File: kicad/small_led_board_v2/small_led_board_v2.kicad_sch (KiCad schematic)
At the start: 83 parts, among them Q1 SQ2351CES, Q2 SQ2351CES, Q3 SQ2351CES, Q4 SQ2351CES, Q5 SQ2351CES, Q6 SQ2351CES, U1 TPIC6B595N, U2 74HCT595, U3 74AHCT541

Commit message: small led board v2: schematics done for now
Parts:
- C1: renamed from C4; footprint (none) -> Capacitor_THT:C_Disc_D4.7mm_W2.5mm_P5.00mm
- C2: renamed from C1; footprint (none) -> Capacitor_THT:C_Disc_D4.7mm_W2.5mm_P5.00mm
- C3: renamed from C2; footprint (none) -> Capacitor_THT:C_Disc_D4.7mm_W2.5mm_P5.00mm
- J1: renamed from J3; footprint Connector_PinHeader_1.00mm:PinHeader_1x02_P1.00mm_Horizontal -> Connector_PinHeader_2.54mm:PinHeader_1x02_P2.54mm_Horizontal
- J2: footprint (none) -> Connector_BarrelJack:BarrelJack_Horizontal
- J3: renamed from J4; footprint (none) -> Connector_PinSocket_2.54mm:PinSocket_2x05_P2.54mm_Horizontal
- R1: renamed from R16; footprint (none) -> Resistor_THT:R_Axial_DIN0207_L6.3mm_D2.5mm_P7.62mm_Horizontal
- R10: renamed from R12; footprint (none) -> Resistor_THT:R_Axial_DIN0207_L6.3mm_D2.5mm_P7.62mm_Horizontal
- R11: renamed from R13; footprint (none) -> Resistor_THT:R_Axial_DIN0207_L6.3mm_D2.5mm_P7.62mm_Horizontal
- R12: renamed from R14; footprint (none) -> Resistor_THT:R_Axial_DIN0207_L6.3mm_D2.5mm_P7.62mm_Horizontal
- R13: renamed from R1; footprint (none) -> Resistor_THT:R_Axial_DIN0207_L6.3mm_D2.5mm_P7.62mm_Horizontal
- R14: renamed from R2; footprint (none) -> Resistor_THT:R_Axial_DIN0207_L6.3mm_D2.5mm_P7.62mm_Horizontal
- R15: renamed from R3; footprint (none) -> Resistor_THT:R_Axial_DIN0207_L6.3mm_D2.5mm_P7.62mm_Horizontal
- R16: renamed from R4; footprint (none) -> Resistor_THT:R_Axial_DIN0207_L6.3mm_D2.5mm_P7.62mm_Horizontal
- R17: renamed from R5; footprint (none) -> Resistor_THT:R_Axial_DIN0207_L6.3mm_D2.5mm_P7.62mm_Horizontal
- R18: renamed from R6; footprint (none) -> Resistor_THT:R_Axial_DIN0207_L6.3mm_D2.5mm_P7.62mm_Horizontal
- R19: renamed from R7; footprint (none) -> Resistor_THT:R_Axial_DIN0207_L6.3mm_D2.5mm_P7.62mm_Horizontal
- R2: renamed from R15; footprint (none) -> Resistor_THT:R_Axial_DIN0207_L6.3mm_D2.5mm_P7.62mm_Horizontal
- R20: renamed from R8; footprint (none) -> Resistor_THT:R_Axial_DIN0207_L6.3mm_D2.5mm_P7.62mm_Horizontal
- R3: renamed from R17; footprint (none) -> Resistor_THT:R_Axial_DIN0207_L6.3mm_D2.5mm_P7.62mm_Horizontal
- R4: renamed from R18; footprint (none) -> Resistor_THT:R_Axial_DIN0207_L6.3mm_D2.5mm_P7.62mm_Horizontal
- R5: renamed from R19; footprint (none) -> Resistor_THT:R_Axial_DIN0207_L6.3mm_D2.5mm_P7.62mm_Horizontal
- R6: renamed from R20; footprint (none) -> Resistor_THT:R_Axial_DIN0207_L6.3mm_D2.5mm_P7.62mm_Horizontal
- R7: renamed from R9; footprint (none) -> Resistor_THT:R_Axial_DIN0207_L6.3mm_D2.5mm_P7.62mm_Horizontal
- R8: renamed from R10; footprint (none) -> Resistor_THT:R_Axial_DIN0207_L6.3mm_D2.5mm_P7.62mm_Horizontal
- R9: renamed from R11; footprint (none) -> Resistor_THT:R_Axial_DIN0207_L6.3mm_D2.5mm_P7.62mm_Horizontal
- U1: renamed from U3; value 74AHCT541 -> 74HCT541
- renumbered U1 to U3
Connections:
- net +5V: now also C1.1; no longer C1.2
- net ApplyRowAndStrobe': no longer U1.17 (Y1), U3.13 (SRCK)
- net GND: now also C1.2; no longer C1.1
- new net ShiftRowData': U1.17 (Y1), U3.13 (SRCK)
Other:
- note added: "Barrel Jack breaks Pin Header's GND so both can't be used simultaneously."
- note added: "Pin GND refers to FPGA GND."
- note added: "Power Input"
- note removed: "Power Input (5V)"
- moved on the sheet: C1, C2, C3, D1, D10, D11, D12, D13, D14, D15, D16, D17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

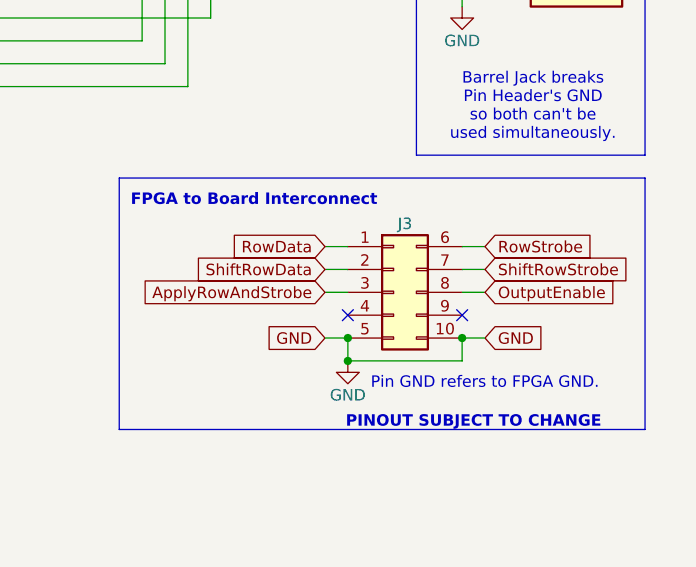
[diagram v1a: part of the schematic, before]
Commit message: small led board v2: fixed wrong connector schematic symbol
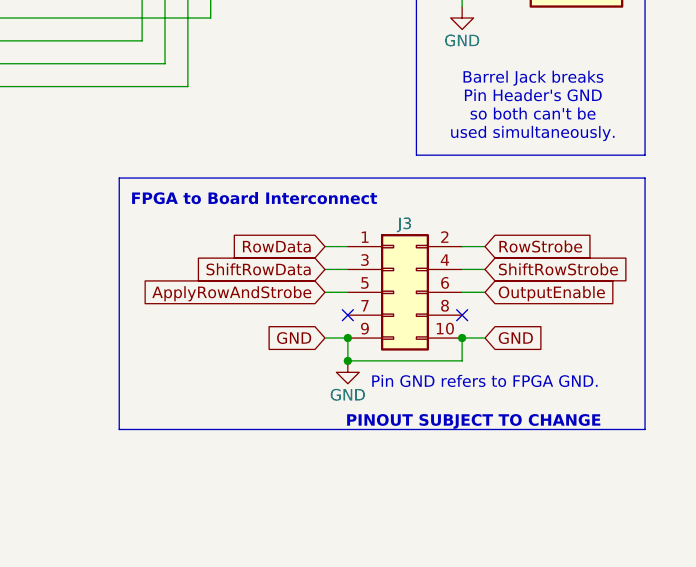
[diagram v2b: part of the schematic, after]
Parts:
- removed J3: ~, Connector_PinSocket_2.54mm:PinSocket_2x05_P2.54mm_Horizontal, symbol Connector_Generic:Conn_02x05_Top_Bottom
- added J3: ~, Connector_PinHeader_2.54mm:PinHeader_2x05_P2.54mm_Horizontal, symbol Connector_Generic:Conn_02x05_Odd_Even
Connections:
- net ApplyRowAndStrobe: now also J3.5 (Pin_5)
- net GND: now also J3.10 (Pin_10), J3.9 (Pin_9)
- net OutputEnable: now also J3.6 (Pin_6)
- net RowData: now also J3.1 (Pin_1)
- net RowStrobe: now also J3.2 (Pin_2)
- net ShiftRowData: now also J3.3 (Pin_3)
- net ShiftRowStrobe: now also J3.4 (Pin_4)
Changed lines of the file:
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@@
 	)
 	(junction
+		(at 261.62 152.4)
+		(diameter 0)
+		(color 0 0 0 0)
+	)
+	(junction
 		(at 124.46 53.34)
 		(diameter 0)
@@
 	)
 	(junction
+		(at 248.92 152.4)
+		(diameter 0)
+		(color 0 0 0 0)
+	)
+	(junction
 		(at 109.22 68.58)
 		(diameter 0)
@@
 	)
 	(junction
-		(at 248.92 152.4)
-		(diameter 0)
-		(color 0 0 0 0)
-	)
-	(junction
 		(at 154.94 99.06)
 		(diameter 0)
@@
 	)
 	(junction
-		(at 261.62 152.4)
-		(diameter 0)
-		(color 0 0 0 0)
-	)
-	(junction
 		(at 40.64 63.5)
 		(diameter 0)
@@
 	)
 	(symbol
-		(lib_id "Connector_Generic:Conn_02x05_Top_Bottom")
-		(at 254 147.32 0)
-		(unit 1)
-		(exclude_from_sim no)
-		(in_bom yes)
-		(on_board yes)
-		(dnp no)
-		(fields_autoplaced yes)
-		(property "Reference" "J3"
-			(at 255.27 139.7 0)
-			(effects
-				(font
-					(size 1.27 1.27)
-				)
-			)
-		)
-		(property "Value" "~"
-			(at 255.27 154.94 0)
-			(effects
-				(font
-					(size 1.27 1.27)
-				)
-			)
-		)
-		(property "Footprint" "Connector_PinSocket_2.54mm:PinSocket_2x05_P2.54mm_Horizontal"
-			(at 254 147.32 0)
-			(effects
-				(font
-					(size 1.27 1.27)
-				)
-				(hide yes)
-			)
-		)
-		(property "Datasheet" "~"
-			(at 254 147.32 0)
-			(effects
-				(font
-					(size 1.27 1.27)
-				)
-				(hide yes)
-			)
-		)
-		(property "Description" "Generic connector, double row, 02x05, top/bottom pin numbering scheme (row 1: 1...pins_per_row, row2: pins_per_row+1 ... num_pins), script generated (kicad-library-utils/schlib/autogen/connector/)"
-			(at 254 147.32 0)
-			(effects
-				(font
-					(size 1.27 1.27)
-				)
-				(hide yes)
-			)
-		)
-		(pin "4"
-		)
-		(pin "6"
-		)
-		(pin "9"
-		)
-		(pin "7"
-		)
-		(pin "8"
-		)
-		(pin "5"
-		)
-		(pin "3"
-		)
-		(pin "10"
-		)
-		(pin "1"
-		)
-		(pin "2"
-		)
-		(instances
-			(project ""
-				(path "/14944b3f-a712-4d15-8930-1f3cb67339bb"
-					(reference "J3")
-					(unit 1)
-				)
-			)
-		)
-	)
-	(symbol
 		(lib_id "Device:LED")
 		(at 67.31 53.34 0)
@@
 					(unit 1)
 				)
+			)
+		)
+	)
+	(symbol
+		(lib_id "Connector_Generic:Conn_02x05_Odd_Even")
+		(at 254 147.32 0)
+		(unit 1)
+		(exclude_from_sim no)
+		(in_bom yes)
+		(on_board yes)
+		(dnp no)
+		(property "Reference" "J3"
+			(at 255.27 139.7 0)
+			(effects
+				(font
+					(size 1.27 1.27)
+				)
+			)
+		)
+		(property "Value" "~"
+			(at 255.27 154.94 0)
+			(effects
+				(font
+					(size 1.27 1.27)
+				)
+			)
+		)
+		(property "Footprint" "Connector_PinHeader_2.54mm:PinHeader_2x05_P2.54mm_Horizontal"
+			(at 254 147.32 0)
+			(effects
+				(font
+					(size 1.27 1.27)
+				)
+				(hide yes)
+			)
+		)
+		(property "Datasheet" "~"
+			(at 254 147.32 0)
+			(effects
+				(font
+					(size 1.27 1.27)
+				)
+				(hide yes)
+			)
+		)
+		(property "Description" "Generic connector, double row, 02x05, odd/even pin numbering scheme (row 1 odd numbers, row 2 even numbers), script generated (kicad-library-utils/schlib/autogen/connector/)"
+			(at 254 147.32 0)
+			(effects
+				(font
+					(size 1.27 1.27)
+				)
+				(hide yes)
+			)
+		)
+		(pin "3"
+		)
+		(pin "6"
+		)
+		(pin "2"
+		)
+		(pin "4"
+		)
+		(pin "7"
+		)
+		(pin "5"
+		)
+		(pin "9"
+		)
+		(pin "10"
+		)
+		(pin "1"
+		)
+		(pin "8"
+		)
+		(instances
+			(project ""
+				(path "/14944b3f-a712-4d15-8930-1f3cb67339bb"
+					(reference "J3")
+					(unit 1)
+				)

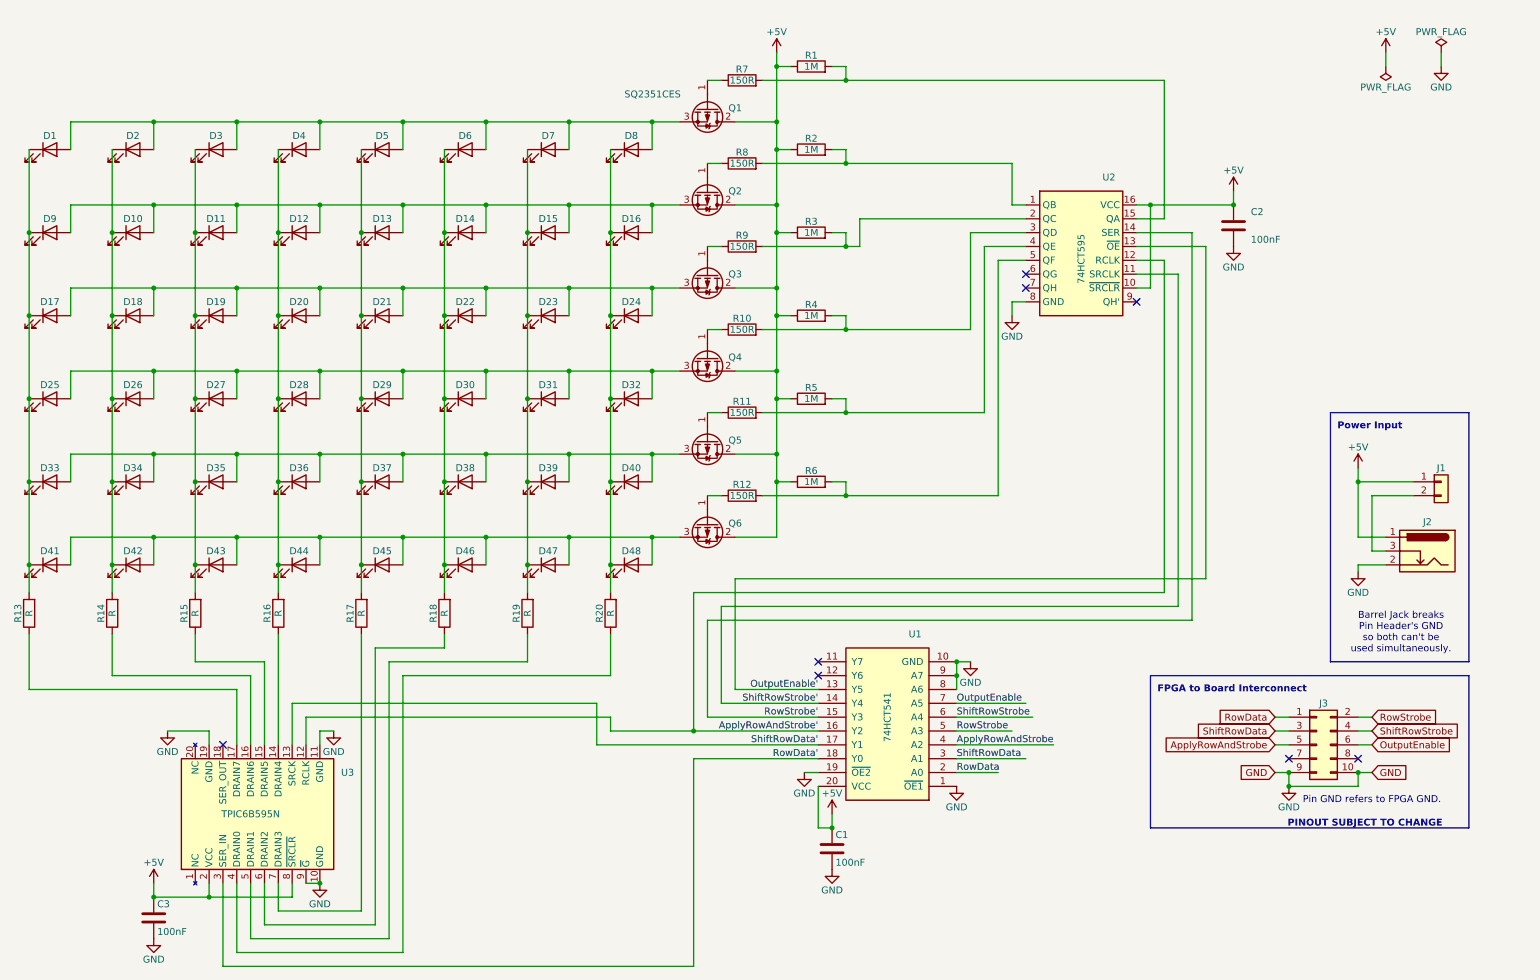
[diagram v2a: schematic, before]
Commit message: small led board v2: added missing pull ups to schematic and pcb
But the ordered PCB is obviously still missing those, they will be soldered on hacky on top just like it was meant to be.
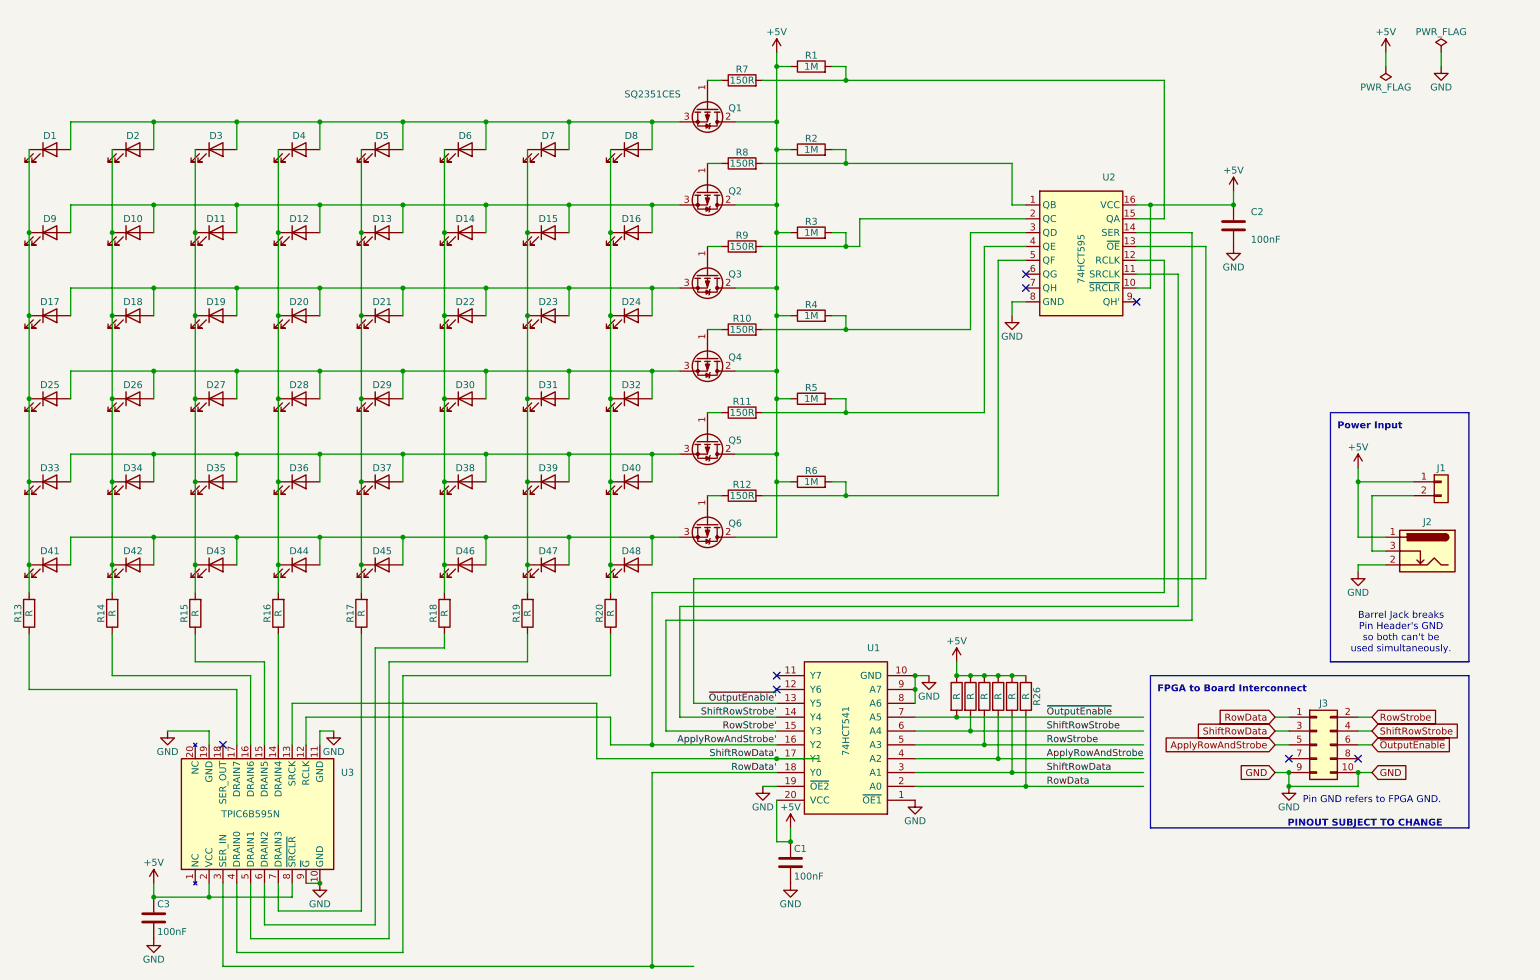
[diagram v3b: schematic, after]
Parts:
- added R21, R22, R23, R24, R25, R26: R, Resistor_THT:R_Axial_DIN0207_L6.3mm_D2.5mm_P7.62mm_Horizontal, symbol Device:R
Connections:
- net +5V: now also R21.1, R22.1, R23.1, R24.1, R25.1, R26.1
- net ApplyRowAndStrobe: now also R24.2
- net RowData: now also R26.2
- net RowStrobe: now also R23.2
- net ShiftRowData: now also R25.2
- net ShiftRowStrobe: now also R22.2
- net OutputEnable renamed ~{OutputEnable}
- net ~{OutputEnable}: now also R21.2
- net OutputEnable' renamed ~{OutputEnable'}
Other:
- moved on the sheet: C1, U1

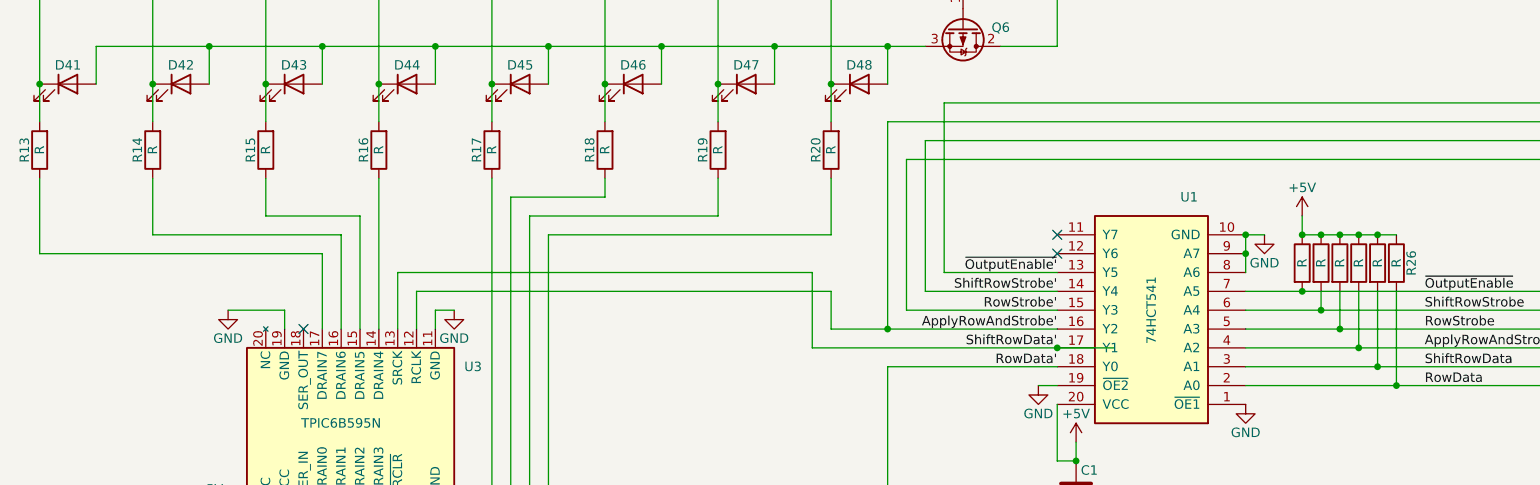
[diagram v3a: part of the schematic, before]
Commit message: small led board v2: updated resistor values
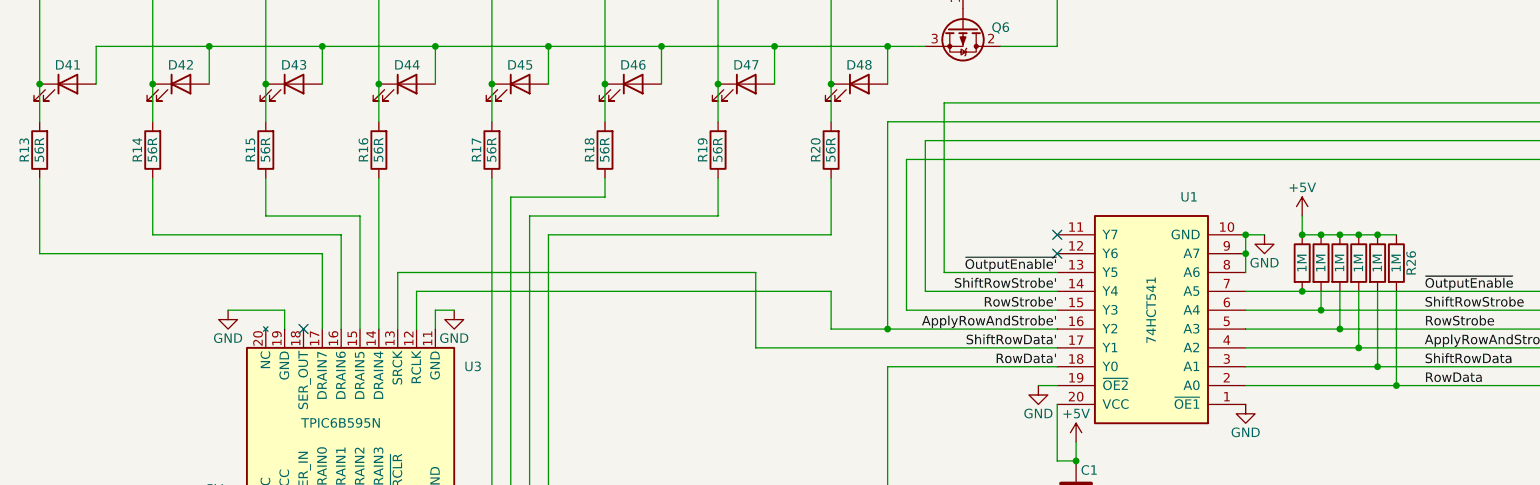
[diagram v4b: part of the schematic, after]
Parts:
- R13, R14, R15, R16, R17, R18, R19, R20: value R -> 56R
- R21, R22, R23, R24, R25, R26: value R -> 1M
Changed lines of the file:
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@@
 	)
 	(junction
-		(at 154.94 149.86)
-		(diameter 0)
-		(color 0 0 0 0)
-	)
-	(junction
 		(at 55.88 48.26)
 		(diameter 0)
@@
 	(wire
 		(pts
-			(xy 121.92 139.7) (xy 121.92 149.86)
+			(xy 114.3 139.7) (xy 114.3 149.86)
 		)
 		(stroke
@@
 	(wire
 		(pts
-			(xy 66.04 139.7) (xy 121.92 139.7)
+			(xy 66.04 139.7) (xy 114.3 139.7)
 		)
 		(stroke
@@
 	(wire
 		(pts
-			(xy 121.92 149.86) (xy 154.94 149.86)
-		)
-		(stroke
-			(width 0)
-			(type default)
-		)
-	)
-	(wire
-		(pts
 			(xy 261.62 96.52) (xy 261.62 99.06)
 		)
@@
 	(wire
 		(pts
-			(xy 154.94 149.86) (xy 162.56 149.86)
+			(xy 114.3 149.86) (xy 154.94 149.86)
 		)
 		(stroke
@@
 			)
 		)
-		(property "Value" "R"
+		(property "Value" "56R"
 			(at 48.26 123.19 90)
 			(effects
@@
 			)
 		)
-		(property "Value" "R"
+		(property "Value" "1M"
 			(at 190.5 138.43 90)
 			(effects
@@
 			)
 		)
-		(property "Value" "R"
+		(property "Value" "56R"
 			(at 93.98 123.19 90)
 			(effects
@@
 			)
 		)
-		(property "Value" "R"
+		(property "Value" "56R"
 			(at 109.22 123.19 90)
 			(effects
@@
 			)
 		)
-		(property "Value" "R"
+		(property "Value" "1M"
 			(at 200.66 138.43 90)
 			(effects
@@
 			)
 		)
-		(property "Value" "R"
+		(property "Value" "1M"
 			(at 193.04 138.43 90)
 			(effects
@@
 			)
 		)
-		(property "Value" "R"
+		(property "Value" "56R"
 			(at 63.5 123.19 90)
 			(effects
@@
 			)
 		)
-		(property "Value" "R"
+		(property "Value" "1M"
 			(at 195.58 138.43 90)
 			(effects
@@
 			)
 		)
-		(property "Value" "R"
+		(property "Value" "56R"
 			(at 124.46 123.19 90)
 			(effects
@@
 			)
 		)
-		(property "Value" "R"
+		(property "Value" "56R"
 			(at 17.78 123.19 90)
 			(effects
@@
 			)
 		)
-		(property "Value" "R"
+		(property "Value" "56R"
 			(at 33.02 123.19 90)
 			(effects
@@
 			)
 		)
-		(property "Value" "R"
+		(property "Value" "1M"
 			(at 198.12 138.43 90)
 			(effects
@@
 			)
 		)
-		(property "Value" "R"
+		(property "Value" "1M"
 			(at 187.96 138.43 90)
 			(effects
@@
 			)
 		)
-		(property "Value" "R"
+		(property "Value" "56R"
 			(at 78.74 123.19 90)
 			(effects
